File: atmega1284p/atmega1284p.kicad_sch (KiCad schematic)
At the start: 38 parts, among them J1 PA, J10 AVR-ISP-6, J11 USB_B_Mini, J12 CC1101_Breakout, J2 PB, J3 PC, J4 PD, J5 I2C1, J6 I2C2, J7 Power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

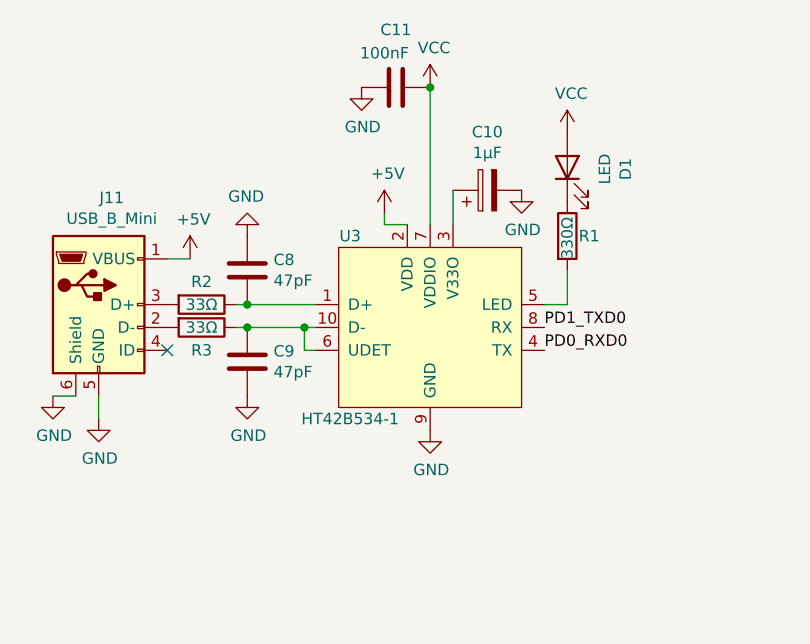
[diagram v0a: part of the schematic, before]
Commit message: atmega1284p: Use CH340N as TTL adapter
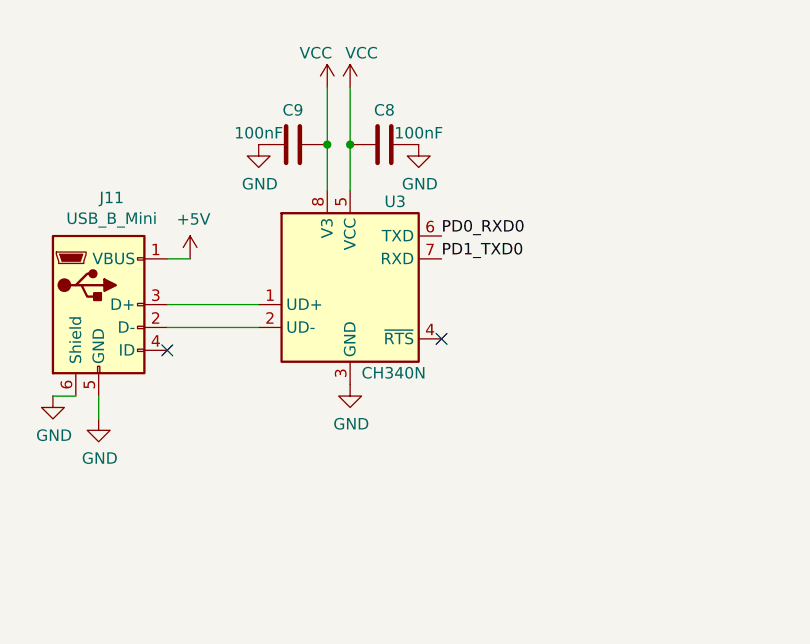
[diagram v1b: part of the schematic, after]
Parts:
- removed C10: 1µF, boards:electrolytic_capacitor_10uf, symbol Device:C_Polarized
- removed C11: 100nF, Capacitor_THT:C_Disc_D4.3mm_W1.9mm_P5.00mm, symbol Device:C
- removed D1: LED, LED_THT:LED_D3.0mm, symbol Device:LED
- removed R1: 330Ω, Resistor_THT:R_Axial_DIN0207_L6.3mm_D2.5mm_P2.54mm_Vertical, symbol Device:R
- removed R2, R3: 33Ω, Resistor_THT:R_Axial_DIN0207_L6.3mm_D2.5mm_P2.54mm_Vertical, symbol Device:R
- removed U3: HT42B534-1, boards:HT42B534-1SOP10, symbol boards:HT42B534-1SOP10
- added U3: CH340N, Package_SO:SOP-8_3.9x4.9mm_P1.27mm, symbol boards:CH340N
- C8, C9: value 47pF -> 100nF
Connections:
- net GND: now also U3.3 (GND)
- net PD0_RXD0: now also U3.6 (TXD)
- net PD1_TXD0: now also U3.7 (RXD)
- net VCC: now also C8.2, C9.1, U3.5 (VCC), U3.8 (V3)
- net at J11.3 (D+): now also U3.1 (UD+)
- net at J11.2 (D-): now also U3.2 (UD-)
- no-connect marks 3 -> 4
